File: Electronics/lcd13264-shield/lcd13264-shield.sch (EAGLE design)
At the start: 54 parts, among them J1 MICRO-SDCARD-CONNECTOR-330006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, J3 ARDUINO_R3_SHIELDUNO_R3_SHIEL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, Q1 PNP-500mA, X1 FH12-12S-1S, X2 FH12-12S-1S

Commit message: Corrected the transistor value. We are using a transistor with built-in base resistor.
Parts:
- Q1: MPN MMBT3906 -> DDTB142TC; OC_DIGIKEY (none) -> DDTB142TC; OC_MOUSER 512-MMBT3906 -> 621-DDTB142TC-F
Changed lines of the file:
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@@
 <grid distance="0.1" unitdist="inch" unit="inch" style="lines" multiple="1" display="no" altdistance="0.01" altunitdist="inch" altunit="inch"/>
 <layers>
-<layer number="1" name="Top" color="4" fill="1" visible="no" active="no"/>
-<layer number="2" name="Route2" color="1" fill="3" visible="no" active="no"/>
-<layer number="3" name="Route3" color="4" fill="3" visible="no" active="no"/>
-<layer number="4" name="Route4" color="1" fill="4" visible="no" active="no"/>
-<layer number="5" name="Route5" color="4" fill="4" visible="no" active="no"/>
-<layer number="6" name="Route6" color="1" fill="8" visible="no" active="no"/>
-<layer number="7" name="Route7" color="4" fill="8" visible="no" active="no"/>
-<layer number="8" name="Route8" color="1" fill="2" visible="no" active="no"/>
-<layer number="9" name="Route9" color="4" fill="2" visible="no" active="no"/>
-<layer number="10" name="Route10" color="1" fill="7" visible="no" active="no"/>
-<layer number="11" name="Route11" color="4" fill="7" visible="no" active="no"/>
-<layer number="12" name="Route12" color="1" fill="5" visible="no" active="no"/>
-<layer number="13" name="Route13" color="4" fill="5" visible="no" active="no"/>
-<layer number="14" name="Route14" color="1" fill="6" visible="no" active="no"/>
-<layer number="15" name="Route15" color="4" fill="6" visible="no" active="no"/>
-<layer number="16" name="Bottom" color="1" fill="1" visible="no" active="no"/>
-<layer number="17" name="Pads" color="2" fill="1" visible="no" active="no"/>
-<layer number="18" name="Vias" color="2" fill="1" visible="no" active="no"/>
-<layer number="19" name="Unrouted" color="6" fill="1" visible="no" active="no"/>
-<layer number="20" name="Dimension" color="13" fill="1" visible="no" active="no"/>
-<layer number="21" name="tPlace" color="7" fill="1" visible="no" active="no"/>
-<layer number="22" name="bPlace" color="14" fill="1" visible="no" active="no"/>
-<layer number="23" name="tOrigins" color="15" fill="1" visible="no" active="no"/>
-<layer number="24" name="bOrigins" color="15" fill="1" visible="no" active="no"/>
-<layer number="25" name="tNames" color="7" fill="1" visible="no" active="no"/>
-<layer number="26" name="bNames" color="7" fill="1" visible="no" active="no"/>
-<layer number="27" name="tValues" color="7" fill="1" visible="no" active="no"/>
-<layer number="28" name="bValues" color="7" fill="1" visible="no" active="no"/>
+<layer number="1" name="Top" color="4" fill="1" visible="yes" active="no"/>
+<layer number="2" name="Route2" color="1" fill="3" visible="yes" active="no"/>
+<layer number="3" name="Route3" color="4" fill="3" visible="yes" active="no"/>
+<layer number="4" name="Route4" color="1" fill="4" visible="yes" active="no"/>
+<layer number="5" name="Route5" color="4" fill="4" visible="yes" active="no"/>
+<layer number="6" name="Route6" color="1" fill="8" visible="yes" active="no"/>
+<layer number="7" name="Route7" color="4" fill="8" visible="yes" active="no"/>
+<layer number="8" name="Route8" color="1" fill="2" visible="yes" active="no"/>
+<layer number="9" name="Route9" color="4" fill="2" visible="yes" active="no"/>
+<layer number="10" name="Route10" color="1" fill="7" visible="yes" active="no"/>
+<layer number="11" name="Route11" color="4" fill="7" visible="yes" active="no"/>
+<layer number="12" name="Route12" color="1" fill="5" visible="yes" active="no"/>
+<layer number="13" name="Route13" color="4" fill="5" visible="yes" active="no"/>
+<layer number="14" name="Route14" color="1" fill="6" visible="yes" active="no"/>
+<layer number="15" name="Route15" color="4" fill="6" visible="yes" active="no"/>
+<layer number="16" name="Bottom" color="1" fill="1" visible="yes" active="no"/>
+<layer number="17" name="Pads" color="2" fill="1" visible="yes" active="no"/>
+<layer number="18" name="Vias" color="2" fill="1" visible="yes" active="no"/>
+<layer number="19" name="Unrouted" color="6" fill="1" visible="yes" active="no"/>
+<layer number="20" name="Dimension" color="13" fill="1" visible="yes" active="no"/>
+<layer number="21" name="tPlace" color="7" fill="1" visible="yes" active="no"/>
+<layer number="22" name="bPlace" color="14" fill="1" visible="yes" active="no"/>
+<layer number="23" name="tOrigins" color="15" fill="1" visible="yes" active="no"/>
+<layer number="24" name="bOrigins" color="15" fill="1" visible="yes" active="no"/>
+<layer number="25" name="tNames" color="7" fill="1" visible="yes" active="no"/>
+<layer number="26" name="bNames" color="7" fill="1" visible="yes" active="no"/>
+<layer number="27" name="tValues" color="7" fill="1" visible="yes" active="no"/>
+<layer number="28" name="bValues" color="7" fill="1" visible="yes" active="no"/>
 <layer number="29" name="tStop" color="7" fill="3" visible="no" active="no"/>
 <layer number="30" name="bStop" color="7" fill="6" visible="no" active="no"/>
@@
 <layer number="35" name="tGlue" color="7" fill="4" visible="no" active="no"/>
 <layer number="36" name="bGlue" color="7" fill="5" visible="no" active="no"/>
-<layer number="37" name="tTest" color="7" fill="1" visible="no" active="no"/>
-<layer number="38" name="bTest" color="7" fill="1" visible="no" active="no"/>
+<layer number="37" name="tTest" color="7" fill="1" visible="yes" active="no"/>
+<layer number="38" name="bTest" color="7" fill="1" visible="yes" active="no"/>
 <layer number="39" name="tKeepout" color="4" fill="11" visible="no" active="no"/>
 <layer number="40" name="bKeepout" color="1" fill="11" visible="no" active="no"/>
@@
 <layer number="44" name="Drills" color="7" fill="1" visible="no" active="no"/>
 <layer number="45" name="Holes" color="7" fill="1" visible="no" active="no"/>
-<layer number="46" name="Milling" color="3" fill="1" visible="no" active="no"/>
-<layer number="47" name="Measures" color="7" fill="1" visible="no" active="no"/>
-<layer number="48" name="Document" color="7" fill="1" visible="no" active="no"/>
-<layer number="49" name="Reference" color="7" fill="1" visible="no" active="no"/>
-<layer number="50" name="dxf" color="7" fill="1" visible="no" active="no"/>
-<layer number="51" name="tDocu" color="6" fill="1" visible="no" active="no"/>
-<layer number="52" name="bDocu" color="7" fill="1" visible="no" active="no"/>
-<layer number="53" name="tGND_GNDA" color="7" fill="9" visible="no" active="no"/>
-<layer number="54" name="bGND_GNDA" color="1" fill="9" visible="no" active="no"/>
-<layer number="56" name="wert" color="7" fill="1" visible="no" active="no"/>
-<layer number="57" name="tCAD" color="7" fill="1" visible="no" active="no"/>
-<layer number="59" name="tCarbon" color="7" fill="1" visible="no" active="no"/>
-<layer number="60" name="bCarbon" color="7" fill="1" visible="no" active="no"/>
+<layer number="46" name="Milling" color="3" fill="1" visible="yes" active="no"/>
+<layer number="47" name="Measures" color="7" fill="1" visible="yes" active="no"/>
+<layer number="48" name="Document" color="7" fill="1" visible="yes" active="no"/>
+<layer number="49" name="Reference" color="7" fill="1" visible="yes" active="no"/>
+<layer number="50" name="dxf" color="7" fill="1" visible="yes" active="no"/>
+<layer number="51" name="tDocu" color="6" fill="1" visible="yes" active="no"/>
+<layer number="52" name="bDocu" color="7" fill="1" visible="yes" active="no"/>
+<layer number="53" name="tGND_GNDA" color="7" fill="9" visible="yes" active="no"/>
+<layer number="54" name="bGND_GNDA" color="1" fill="9" visible="yes" active="no"/>
+<layer number="56" name="wert" color="7" fill="1" visible="yes" active="no"/>
+<layer number="57" name="tCAD" color="7" fill="1" visible="yes" active="no"/>
+<layer number="59" name="tCarbon" color="7" fill="1" visible="yes" active="no"/>
+<layer number="60" name="bCarbon" color="7" fill="1" visible="yes" active="no"/>
 <layer number="90" name="Modules" color="5" fill="1" visible="yes" active="yes"/>
 <layer number="91" name="Nets" color="2" fill="1" visible="yes" active="yes"/>
@@
 <part name="SUPPLY3" library="SparkFun-Aesthetics" deviceset="5V" device=""/>
 <part name="Q1" library="SparkFun-DiscreteSemi" deviceset="TRANSISTOR-PNP-DDTB142TC" device="" value="PNP-500mA">
-<attribute name="MPN" value="MMBT3906"/>
-<attribute name="OC_MOUSER" value="512-MMBT3906"/>
+<attribute name="MPN" value="DDTB142TC"/>
+<attribute name="OC_DIGIKEY" value="DDTB142TC"/>
+<attribute name="OC_MOUSER" value="621-DDTB142TC-F"/>
 </part>
 <part name="P+5" library="SparkFun" deviceset="3.3V" device=""/>
@@
 <attribute name="MPN" x="170.18" y="139.7" size="1.778" layer="96" rot="MR0" display="off"/>
 <attribute name="OC_MOUSER" x="170.18" y="139.7" size="1.778" layer="96" rot="MR0" display="off"/>
+<attribute name="OC_DIGIKEY" x="170.18" y="139.7" size="1.778" layer="96" rot="MR0" display="off"/>
 </instance>
 <instance part="P+5" gate="G$1" x="167.64" y="149.86"/>

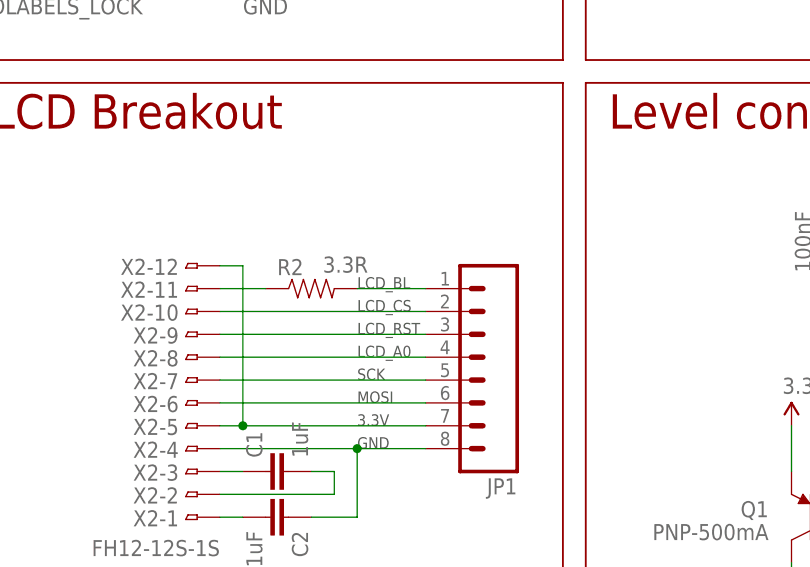
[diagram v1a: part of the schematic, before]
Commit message: Added active low notation to LCD_BL.
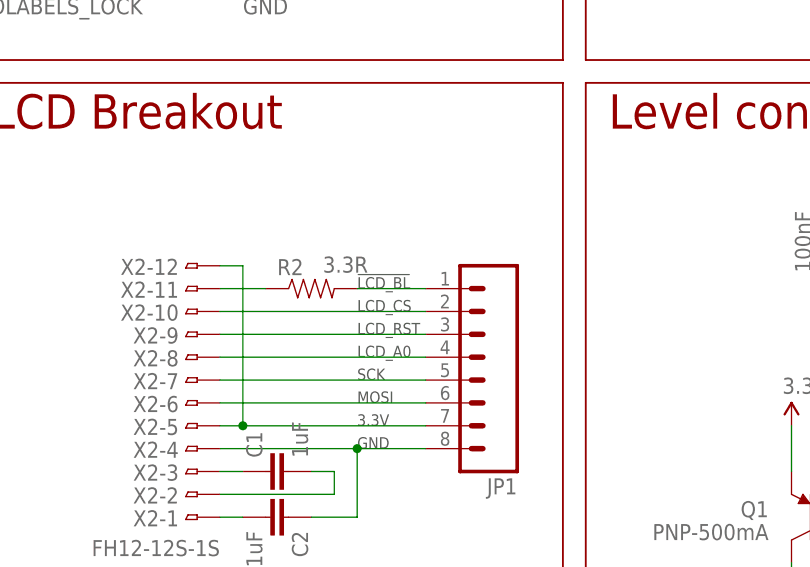
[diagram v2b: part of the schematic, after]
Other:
- note added: "!LCD_BL"
- note removed: "LCD_BL"
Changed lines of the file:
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@@
 <grid distance="0.1" unitdist="inch" unit="inch" style="lines" multiple="1" display="no" altdistance="0.01" altunitdist="inch" altunit="inch"/>
 <layers>
-<layer number="1" name="Top" color="4" fill="1" visible="yes" active="no"/>
-<layer number="2" name="Route2" color="1" fill="3" visible="yes" active="no"/>
-<layer number="3" name="Route3" color="4" fill="3" visible="yes" active="no"/>
-<layer number="4" name="Route4" color="1" fill="4" visible="yes" active="no"/>
-<layer number="5" name="Route5" color="4" fill="4" visible="yes" active="no"/>
-<layer number="6" name="Route6" color="1" fill="8" visible="yes" active="no"/>
-<layer number="7" name="Route7" color="4" fill="8" visible="yes" active="no"/>
-<layer number="8" name="Route8" color="1" fill="2" visible="yes" active="no"/>
-<layer number="9" name="Route9" color="4" fill="2" visible="yes" active="no"/>
-<layer number="10" name="Route10" color="1" fill="7" visible="yes" active="no"/>
-<layer number="11" name="Route11" color="4" fill="7" visible="yes" active="no"/>
-<layer number="12" name="Route12" color="1" fill="5" visible="yes" active="no"/>
-<layer number="13" name="Route13" color="4" fill="5" visible="yes" active="no"/>
-<layer number="14" name="Route14" color="1" fill="6" visible="yes" active="no"/>
-<layer number="15" name="Route15" color="4" fill="6" visible="yes" active="no"/>
-<layer number="16" name="Bottom" color="1" fill="1" visible="yes" active="no"/>
-<layer number="17" name="Pads" color="2" fill="1" visible="yes" active="no"/>
-<layer number="18" name="Vias" color="2" fill="1" visible="yes" active="no"/>
-<layer number="19" name="Unrouted" color="6" fill="1" visible="yes" active="no"/>
-<layer number="20" name="Dimension" color="13" fill="1" visible="yes" active="no"/>
-<layer number="21" name="tPlace" color="7" fill="1" visible="yes" active="no"/>
-<layer number="22" name="bPlace" color="14" fill="1" visible="yes" active="no"/>
-<layer number="23" name="tOrigins" color="15" fill="1" visible="yes" active="no"/>
-<layer number="24" name="bOrigins" color="15" fill="1" visible="yes" active="no"/>
-<layer number="25" name="tNames" color="7" fill="1" visible="yes" active="no"/>
-<layer number="26" name="bNames" color="7" fill="1" visible="yes" active="no"/>
-<layer number="27" name="tValues" color="7" fill="1" visible="yes" active="no"/>
-<layer number="28" name="bValues" color="7" fill="1" visible="yes" active="no"/>
+<layer number="1" name="Top" color="4" fill="1" visible="no" active="no"/>
+<layer number="2" name="Route2" color="1" fill="3" visible="no" active="no"/>
+<layer number="3" name="Route3" color="4" fill="3" visible="no" active="no"/>
+<layer number="4" name="Route4" color="1" fill="4" visible="no" active="no"/>
+<layer number="5" name="Route5" color="4" fill="4" visible="no" active="no"/>
+<layer number="6" name="Route6" color="1" fill="8" visible="no" active="no"/>
+<layer number="7" name="Route7" color="4" fill="8" visible="no" active="no"/>
+<layer number="8" name="Route8" color="1" fill="2" visible="no" active="no"/>
+<layer number="9" name="Route9" color="4" fill="2" visible="no" active="no"/>
+<layer number="10" name="Route10" color="1" fill="7" visible="no" active="no"/>
+<layer number="11" name="Route11" color="4" fill="7" visible="no" active="no"/>
+<layer number="12" name="Route12" color="1" fill="5" visible="no" active="no"/>
+<layer number="13" name="Route13" color="4" fill="5" visible="no" active="no"/>
+<layer number="14" name="Route14" color="1" fill="6" visible="no" active="no"/>
+<layer number="15" name="Route15" color="4" fill="6" visible="no" active="no"/>
+<layer number="16" name="Bottom" color="1" fill="1" visible="no" active="no"/>
+<layer number="17" name="Pads" color="2" fill="1" visible="no" active="no"/>
+<layer number="18" name="Vias" color="2" fill="1" visible="no" active="no"/>
+<layer number="19" name="Unrouted" color="6" fill="1" visible="no" active="no"/>
+<layer number="20" name="Dimension" color="13" fill="1" visible="no" active="no"/>
+<layer number="21" name="tPlace" color="7" fill="1" visible="no" active="no"/>
+<layer number="22" name="bPlace" color="14" fill="1" visible="no" active="no"/>
+<layer number="23" name="tOrigins" color="15" fill="1" visible="no" active="no"/>
+<layer number="24" name="bOrigins" color="15" fill="1" visible="no" active="no"/>
+<layer number="25" name="tNames" color="7" fill="1" visible="no" active="no"/>
+<layer number="26" name="bNames" color="7" fill="1" visible="no" active="no"/>
+<layer number="27" name="tValues" color="7" fill="1" visible="no" active="no"/>
+<layer number="28" name="bValues" color="7" fill="1" visible="no" active="no"/>
 <layer number="29" name="tStop" color="7" fill="3" visible="no" active="no"/>
 <layer number="30" name="bStop" color="7" fill="6" visible="no" active="no"/>
@@
 <layer number="35" name="tGlue" color="7" fill="4" visible="no" active="no"/>
 <layer number="36" name="bGlue" color="7" fill="5" visible="no" active="no"/>
-<layer number="37" name="tTest" color="7" fill="1" visible="yes" active="no"/>
-<layer number="38" name="bTest" color="7" fill="1" visible="yes" active="no"/>
+<layer number="37" name="tTest" color="7" fill="1" visible="no" active="no"/>
+<layer number="38" name="bTest" color="7" fill="1" visible="no" active="no"/>
 <layer number="39" name="tKeepout" color="4" fill="11" visible="no" active="no"/>
 <layer number="40" name="bKeepout" color="1" fill="11" visible="no" active="no"/>
@@
 <layer number="44" name="Drills" color="7" fill="1" visible="no" active="no"/>
 <layer number="45" name="Holes" color="7" fill="1" visible="no" active="no"/>
-<layer number="46" name="Milling" color="3" fill="1" visible="yes" active="no"/>
-<layer number="47" name="Measures" color="7" fill="1" visible="yes" active="no"/>
-<layer number="48" name="Document" color="7" fill="1" visible="yes" active="no"/>
-<layer number="49" name="Reference" color="7" fill="1" visible="yes" active="no"/>
-<layer number="50" name="dxf" color="7" fill="1" visible="yes" active="no"/>
-<layer number="51" name="tDocu" color="6" fill="1" visible="yes" active="no"/>
-<layer number="52" name="bDocu" color="7" fill="1" visible="yes" active="no"/>
-<layer number="53" name="tGND_GNDA" color="7" fill="9" visible="yes" active="no"/>
-<layer number="54" name="bGND_GNDA" color="1" fill="9" visible="yes" active="no"/>
-<layer number="56" name="wert" color="7" fill="1" visible="yes" active="no"/>
-<layer number="57" name="tCAD" color="7" fill="1" visible="yes" active="no"/>
-<layer number="59" name="tCarbon" color="7" fill="1" visible="yes" active="no"/>
-<layer number="60" name="bCarbon" color="7" fill="1" visible="yes" active="no"/>
+<layer number="46" name="Milling" color="3" fill="1" visible="no" active="no"/>
+<layer number="47" name="Measures" color="7" fill="1" visible="no" active="no"/>
+<layer number="48" name="Document" color="7" fill="1" visible="no" active="no"/>
+<layer number="49" name="Reference" color="7" fill="1" visible="no" active="no"/>
+<layer number="50" name="dxf" color="7" fill="1" visible="no" active="no"/>
+<layer number="51" name="tDocu" color="6" fill="1" visible="no" active="no"/>
+<layer number="52" name="bDocu" color="7" fill="1" visible="no" active="no"/>
+<layer number="53" name="tGND_GNDA" color="7" fill="9" visible="no" active="no"/>
+<layer number="54" name="bGND_GNDA" color="1" fill="9" visible="no" active="no"/>
+<layer number="56" name="wert" color="7" fill="1" visible="no" active="no"/>
+<layer number="57" name="tCAD" color="7" fill="1" visible="no" active="no"/>
+<layer number="59" name="tCarbon" color="7" fill="1" visible="no" active="no"/>
+<layer number="60" name="bCarbon" color="7" fill="1" visible="no" active="no"/>
 <layer number="90" name="Modules" color="5" fill="1" visible="yes" active="yes"/>
 <layer number="91" name="Nets" color="2" fill="1" visible="yes" active="yes"/>
@@
 <text x="119.38" y="160.02" size="1.27" layer="97">LCD_RST</text>
 <text x="119.38" y="162.56" size="1.27" layer="97">LCD_CS</text>
-<text x="119.38" y="165.1" size="1.27" layer="97">LCD_BL</text>
+<text x="119.38" y="165.1" size="1.27" layer="97">!LCD_BL</text>
 <wire x1="144.78" y1="187.96" x2="297.18" y2="187.96" width="0.2032" layer="94"/>
 <wire x1="144.78" y1="187.96" x2="144.78" y2="124.46" width="0.2032" layer="94"/>

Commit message: Added psrt numbers.
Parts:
- U2, U3: MPN (none) -> TXB0104DR; OC_DIGIKEY (none) -> 296-21928-2-ND
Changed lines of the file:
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@@
 <?xml version="1.0" encoding="utf-8"?>
 <!DOCTYPE eagle SYSTEM "eagle.dtd">
-<eagle version="7.2.0">
+<eagle version="6.5.0">
 <drawing>
 <settings>
@@
 <part name="X2" library="PaxInstrument-T400" deviceset="FH12-12S-1S" device=""/>
 <part name="JP1" library="SparkFun-Connectors" deviceset="M08" device=""/>
-<part name="U2" library="SparkFun-DigitalIC" deviceset="TXB0104PWR" device="SOIC14"/>
-<part name="U3" library="SparkFun-DigitalIC" deviceset="TXB0104PWR" device="SOIC14"/>
+<part name="U2" library="SparkFun-DigitalIC" deviceset="TXB0104PWR" device="SOIC14">
+<attribute name="MPN" value="TXB0104DR"/>
+<attribute name="OC_DIGIKEY" value="296-21928-2-ND"/>
+</part>
+<part name="U3" library="SparkFun-DigitalIC" deviceset="TXB0104PWR" device="SOIC14">
+<attribute name="MPN" value="TXB0104DR"/>
+<attribute name="OC_DIGIKEY" value="296-21928-2-ND"/>
+</part>
 <part name="GND2" library="SparkFun-Aesthetics" deviceset="GND" device=""/>
 <part name="GND3" library="SparkFun-Aesthetics" deviceset="GND" device=""/>
@@
 <instance part="X2" gate="-12" x="101.6" y="167.64" rot="R180"/>
 <instance part="JP1" gate="G$1" x="132.08" y="157.48" rot="R180"/>
-<instance part="U2" gate="G$1" x="203.2" y="149.86"/>
-<instance part="U3" gate="G$1" x="264.16" y="149.86"/>
+<instance part="U2" gate="G$1" x="203.2" y="149.86">
+<attribute name="MPN" x="203.2" y="149.86" size="1.778" layer="96" display="off"/>
+<attribute name="OC_DIGIKEY" x="203.2" y="149.86" size="1.778" layer="96" display="off"/>
+</instance>
+<instance part="U3" gate="G$1" x="264.16" y="149.86">
+<attribute name="MPN" x="264.16" y="149.86" size="1.778" layer="96" display="off"/>
+<attribute name="OC_DIGIKEY" x="264.16" y="149.86" size="1.778" layer="96" display="off"/>
+</instance>
 <instance part="GND2" gate="1" x="203.2" y="129.54"/>
 <instance part="GND3" gate="1" x="264.16" y="129.54"/>
